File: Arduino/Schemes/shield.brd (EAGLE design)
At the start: 44 x 53.5 mm, 10 parts

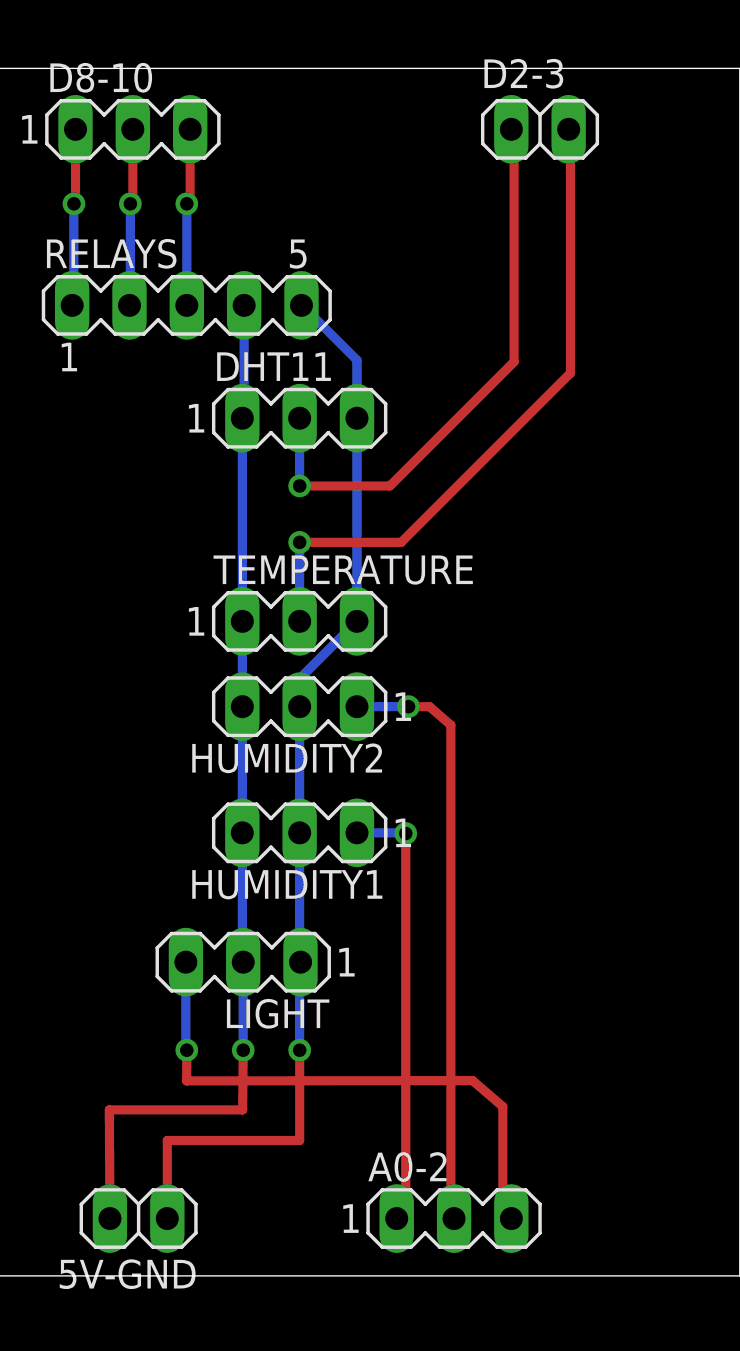
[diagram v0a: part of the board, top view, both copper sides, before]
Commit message: relay board's scheme, shield with optional DHTxx
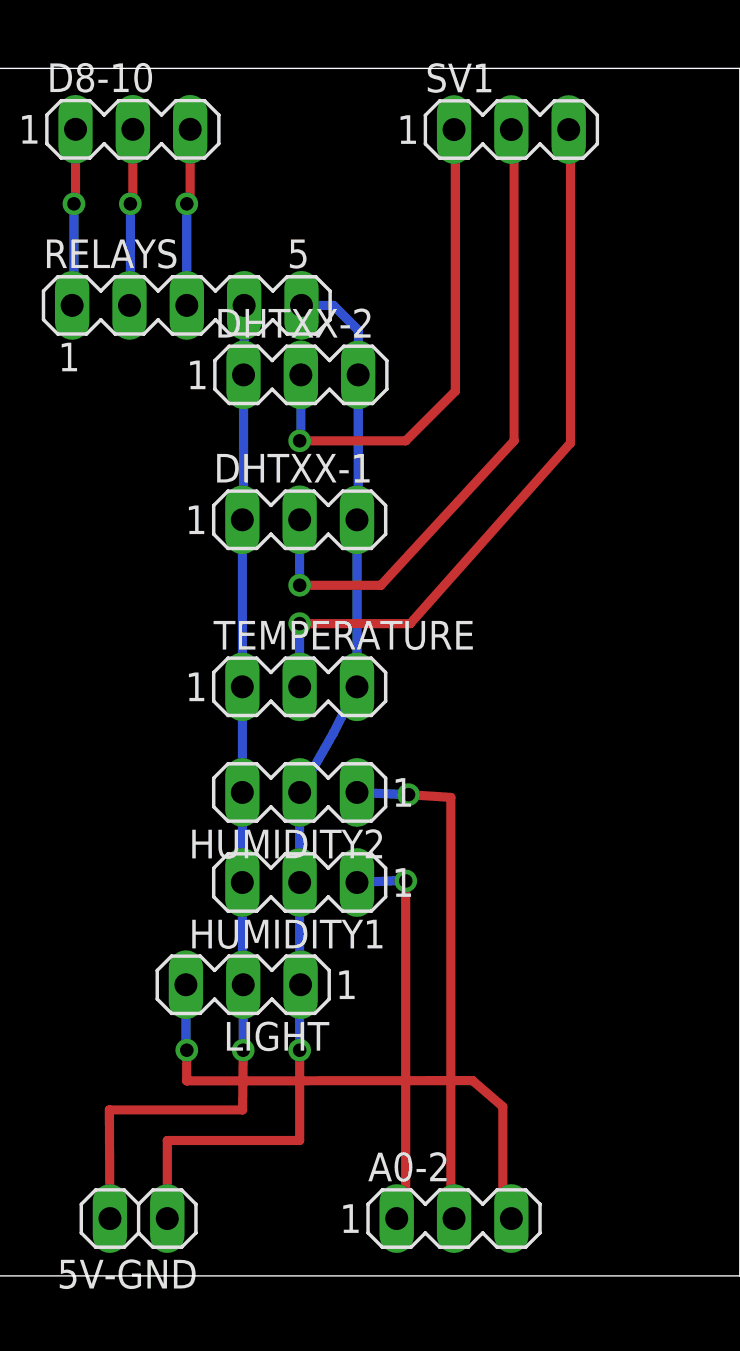
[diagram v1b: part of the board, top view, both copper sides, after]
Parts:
- removed D2-3: (no value), pinhead:1X02
- removed DHT11: (no value), con-lstb:MA03-1
- added DHTXX-1, DHTXX-2, SV1: (no value), con-lstb:MA03-1
- moved HUMIDITY2 3.80 mm to (46.5, 21.4)
- moved TEMPERATURE 2.90 mm to (46.5, 26.1)
- moved HUMIDITY1 2.20 mm to (46.5, 17.4)
- moved LIGHT 1.00 mm to (44.0, 12.9)
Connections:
- new net N$9: DHTXX-2.2, SV1.1
- net GND: now also DHTXX-1.3, DHTXX-2.3; no longer DHT11.3
- net N$1: now also DHTXX-1.2, SV1.2; no longer D2-3.1, DHT11.2
- net N$2: now also SV1.3; no longer D2-3.2
- net VDD: now also DHTXX-1.1, DHTXX-2.1; no longer DHT11.1
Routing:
- net N$9: track 0.00 -> 22.4 mm, vias 0 -> 1
- net N$1: track 25.1 -> 28.9 mm
- net N$5: track 26.4 -> 22.9 mm
- net N$2: track 29.4 -> 32.2 mm
- net GND: track 48.5 -> 50.9 mm
- net N$3: track 19.4 -> 17.3 mm
- net N$7: track 24.8 -> 23.8 mm
